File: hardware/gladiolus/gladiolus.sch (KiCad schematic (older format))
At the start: 94 parts, among them J1 NEIGHBOR1, J2 NEIGHBOR2, J7 BONUS_ROW, Q1 Q_NPN_BEC, U1 THS4520RGT, U2 AD8330ARQZ, U3 AD9283

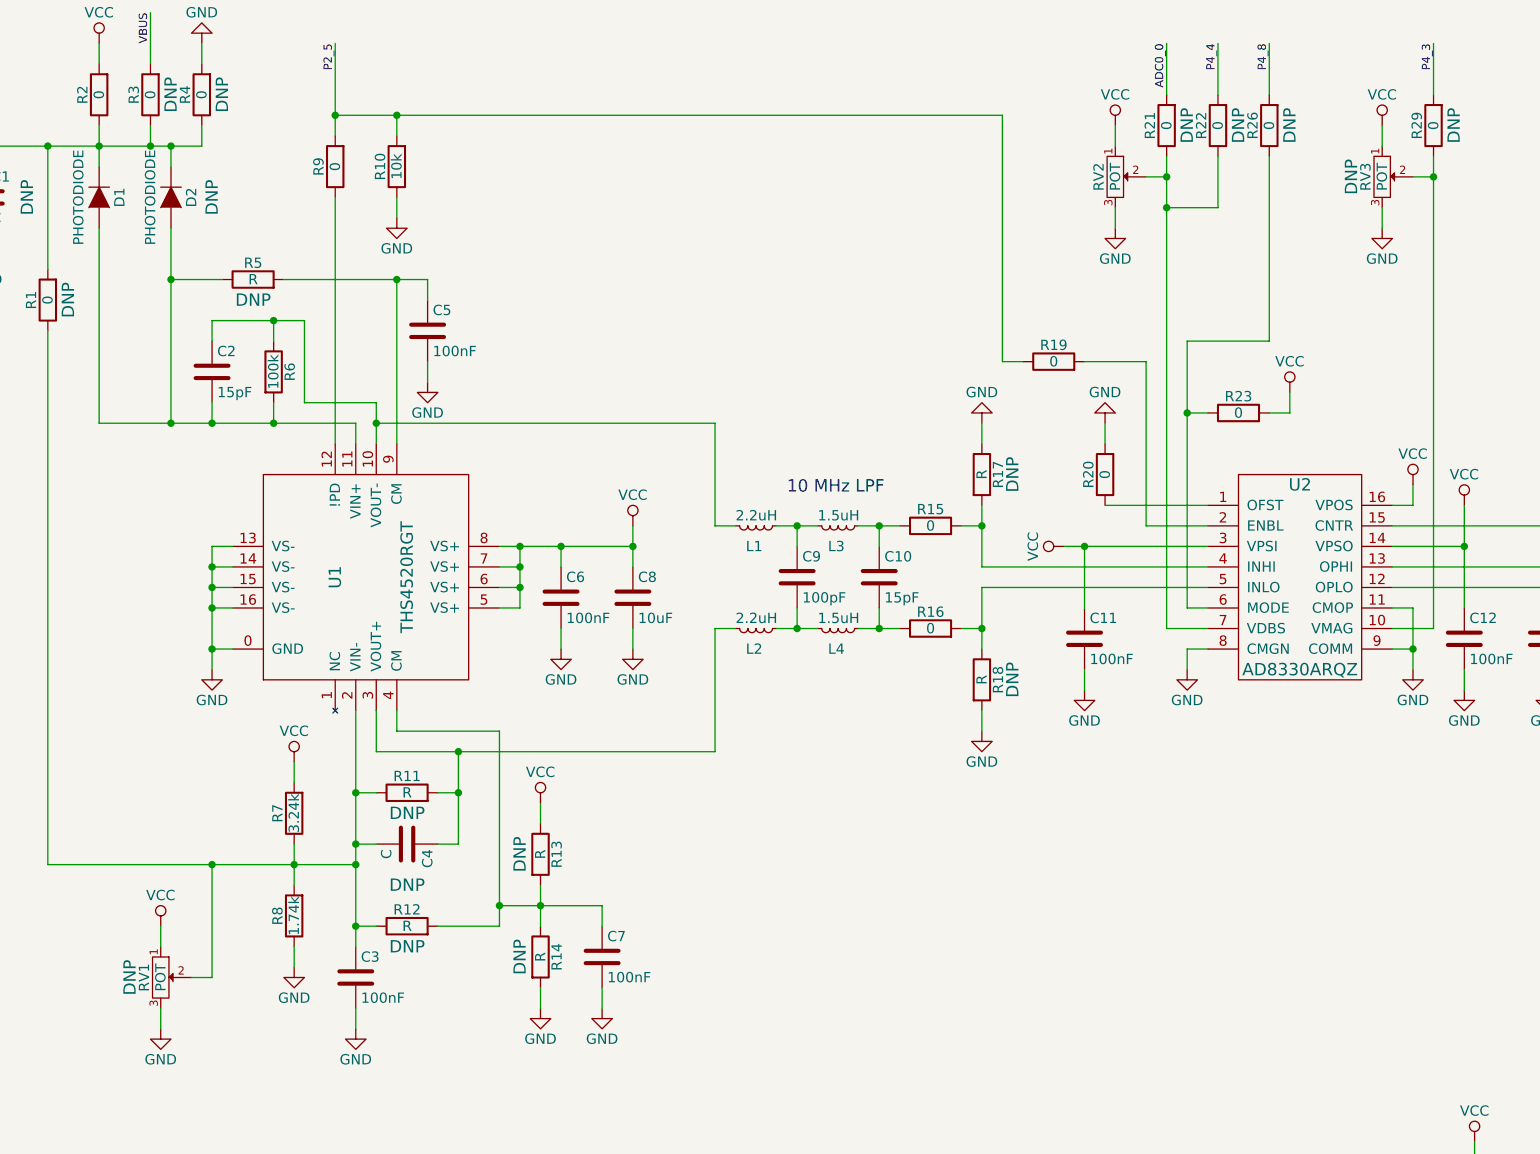
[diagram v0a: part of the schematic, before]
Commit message: Gladiolus: reversed potentiometers
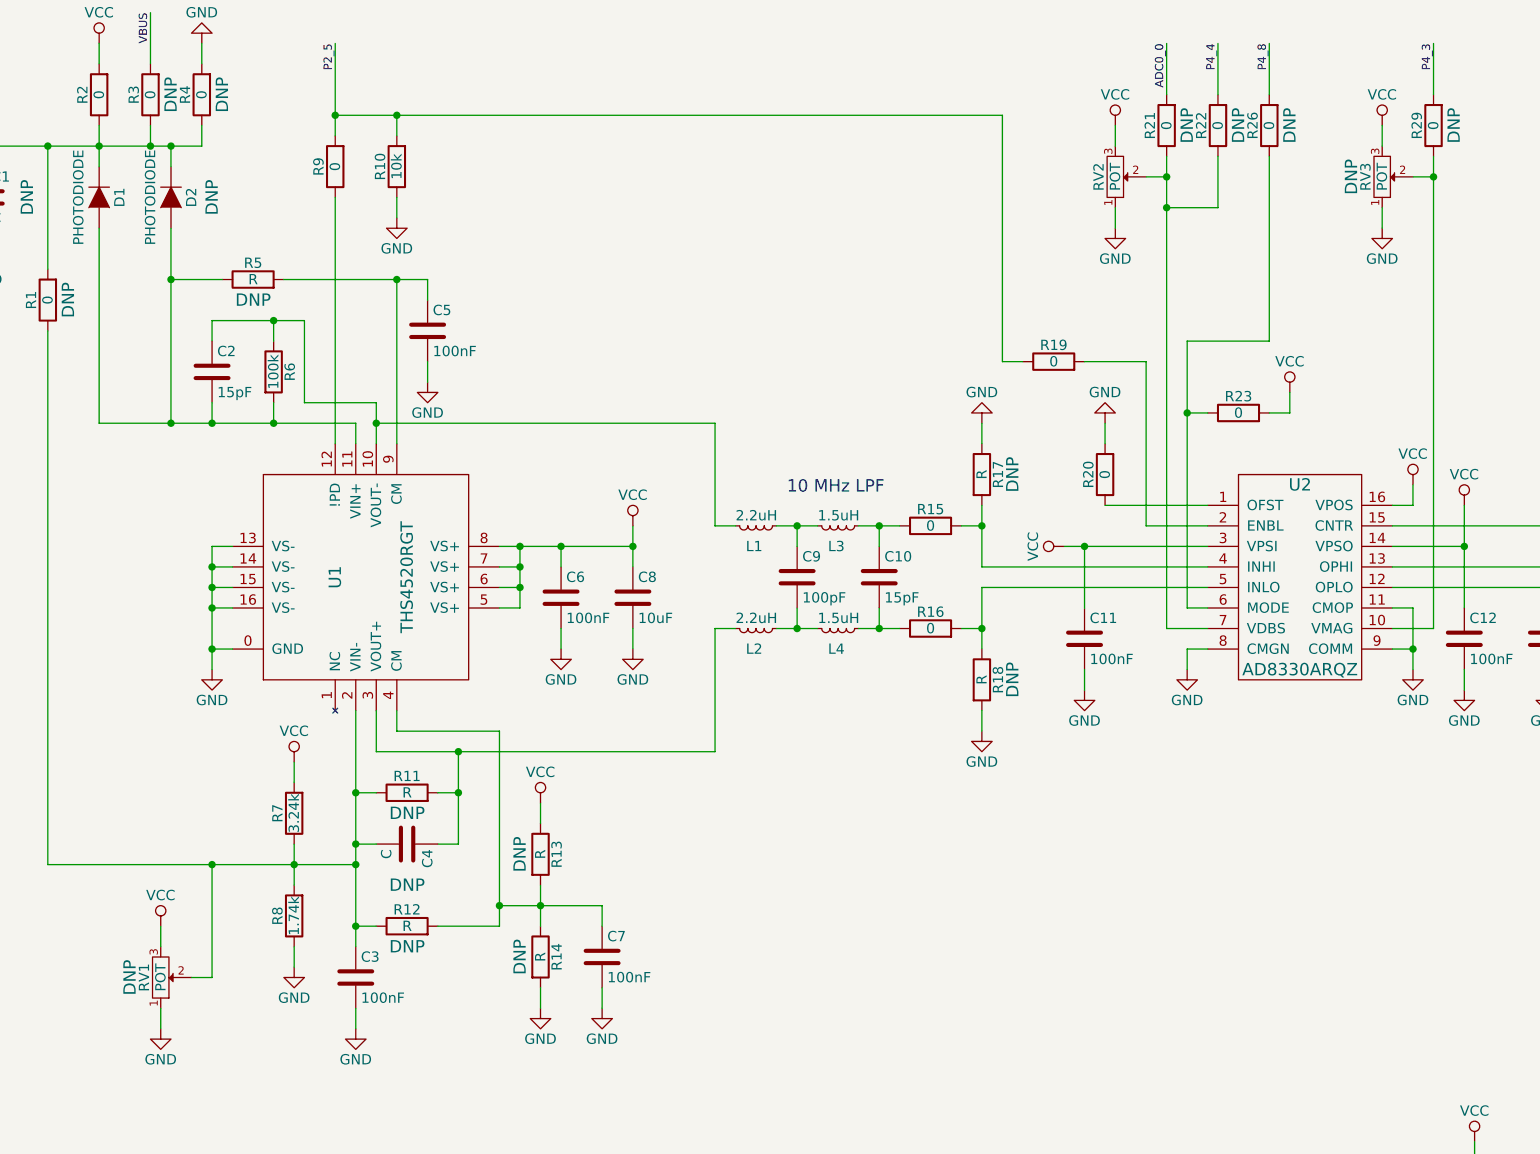
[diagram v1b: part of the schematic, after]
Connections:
- net GND: now also RV1.1, RV2.1, RV3.1; no longer RV1.3, RV2.3, RV3.3
- net VCC: now also RV1.3, RV2.3, RV3.3; no longer RV1.1, RV2.1, RV3.1
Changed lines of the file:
@@
 F 7 "DNP" H 7900 1800 60  0000 C CNN "Note"
 	1    7900 1950
-	0    1    1    0
+	0    1    -1   0
 $EndComp
 $Comp
@@
 F 6 "10k Ohm 0.2W, 1/5W PC Pins Through Hole Trimmer Potentiometer Cermet 1 Turn Top Adjustment" H 6600 1950 60  0001 C CNN "Description"
 	1    6600 1950
-	0    1    1    0
+	0    1    -1   0
 $EndComp
 $Comp
@@
 F 7 "DNP" H 1950 5700 60  0000 C CNN "Note"
 	1    1950 5850
-	0    1    1    0
+	0    1    -1   0
 $EndComp
 Text Label 13800 3100 2    40   ~ 0

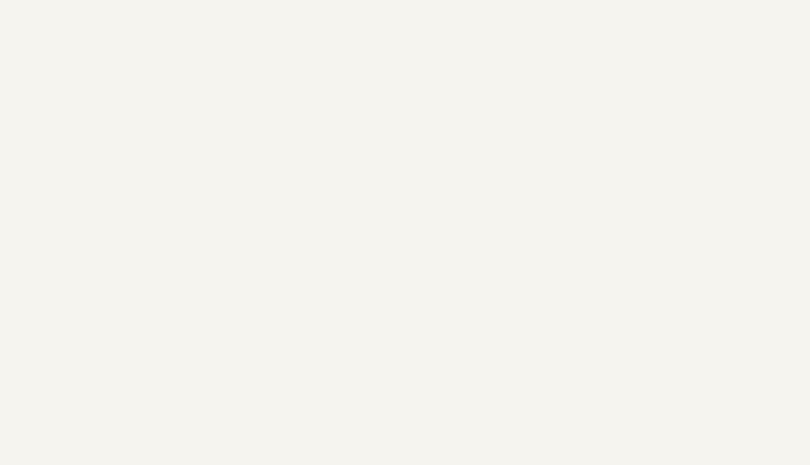
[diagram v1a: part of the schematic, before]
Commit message: Gladiolus: added female header to block direct TX to RX light
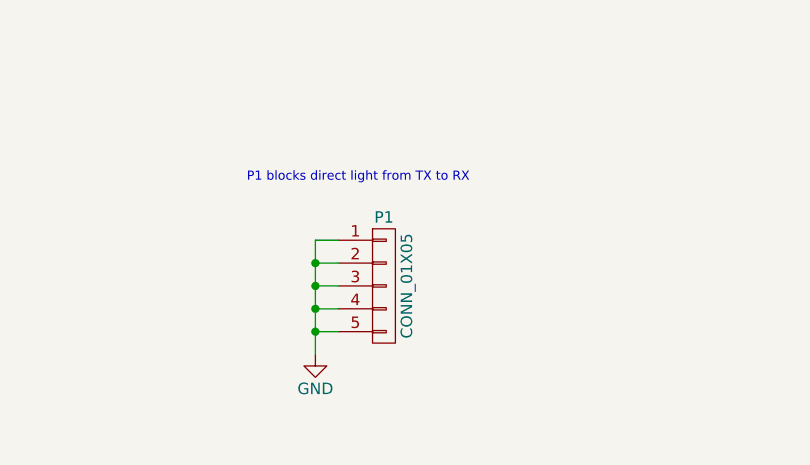
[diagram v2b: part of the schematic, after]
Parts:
- added P1: CONN_01X05, gsg-modules:HEADER-1x5, symbol CONN_01X05
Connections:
- net GND: now also P1.1 (P1), P1.2 (P2), P1.3 (P3), P1.4 (P4), P1.5 (P5)
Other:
- note added: "P1 blocks direct light from TX to RX"
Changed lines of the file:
@@
 Wire Wire Line
 	11600 4250 11600 5450
+$Comp
+L CONN_01X05 P1
+U 1 1 585CA618
+P 11600 7650
+F 0 "P1" H 11600 7950 50  0000 C CNN
+F 1 "CONN_01X05" V 11700 7650 50  0000 C CNN
+F 2 "gsg-modules:HEADER-1x5" H 11600 7650 50  0001 C CNN
+F 3 "" H 11600 7650 50  0000 C CNN
+F 4 "Sullins" H 11600 7650 60  0001 C CNN "Manufacturer"
+F 5 "PPTC051LFBN-RC" H 11600 7650 60  0001 C CNN "Part Number"
+F 6 "CONN HEADER FEM 5POS .1\" SGL TIN" H 11600 7650 60  0001 C CNN "Description"
+	1    11600 7650
+	1    0    0    -1
+$EndComp
+$Comp
+L GND #PWR060
+U 1 1 585CA943
+P 11300 7950
+F 0 "#PWR060" H 11300 7700 50  0001 C CNN
+F 1 "GND" H 11300 7800 50  0000 C CNN
+F 2 "" H 11300 7950 50  0000 C CNN
+F 3 "" H 11300 7950 50  0000 C CNN
+	1    11300 7950
+	1    0    0    -1
+$EndComp
+Wire Wire Line
+	11400 7450 11300 7450
+Wire Wire Line
+	11300 7450 11300 7950
+Wire Wire Line
+	11400 7550 11300 7550
+Connection ~ 11300 7550
+Wire Wire Line
+	11300 7650 11400 7650
+Connection ~ 11300 7650
+Wire Wire Line
+	11400 7750 11300 7750
+Connection ~ 11300 7750
+Wire Wire Line
+	11300 7850 11400 7850
+Connection ~ 11300 7850
+Text Notes 11000 7200 0    40   ~ 0
+P1 blocks direct light from TX to RX
 $EndSCHEMATC

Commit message: Gladiolus: corrected part selection for 0402 0 ohm resistors
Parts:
- R1, R19, R2, R20, R21, R22, R23, R24, R25, R26, R29, R3, R31, R4, R9: Description ES SMD 0.0OHM JUMPER 1/10W 0603 -> RES SMD 0.0OHM JUMPER 1/10W 0603
- R15, R16, R32, R33: Description ES SMD 0.0OHM JUMPER 1/10W 0603 -> RES SMD 0.0OHM JUMPER 1/16W 0402; Part Number RC0603JR-070RL -> RC0402JR-070RL
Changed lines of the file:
@@
 F 4 "Yageo" H 1650 1550 60  0001 C CNN "Manufacturer"
 F 5 "RC0603JR-070RL" H 1650 1550 60  0001 C CNN "Part Number"
-F 6 "ES SMD 0.0OHM JUMPER 1/10W 0603" H 1650 1550 60  0001 C CNN "Description"
+F 6 "RES SMD 0.0OHM JUMPER 1/10W 0603" H 1650 1550 60  0001 C CNN "Description"
 	1    1650 1550
 	-1   0    0    1
@@
 F 4 "Yageo" H 1900 1550 60  0001 C CNN "Manufacturer"
 F 5 "RC0603JR-070RL" H 1900 1550 60  0001 C CNN "Part Number"
-F 6 "ES SMD 0.0OHM JUMPER 1/10W 0603" H 1900 1550 60  0001 C CNN "Description"
+F 6 "RES SMD 0.0OHM JUMPER 1/10W 0603" H 1900 1550 60  0001 C CNN "Description"
 F 7 "DNP" V 1800 1550 60  0000 C CNN "Note"
 	1    1900 1550
@@
 F 4 "Yageo" H 2800 1900 60  0001 C CNN "Manufacturer"
 F 5 "RC0603JR-070RL" H 2800 1900 60  0001 C CNN "Part Number"
-F 6 "ES SMD 0.0OHM JUMPER 1/10W 0603" H 2800 1900 60  0001 C CNN "Description"
+F 6 "RES SMD 0.0OHM JUMPER 1/10W 0603" H 2800 1900 60  0001 C CNN "Description"
 	1    2800 1900
 	-1   0    0    1
@@
 F 4 "Yageo" H 7200 3100 60  0001 C CNN "Manufacturer"
 F 5 "RC0603JR-070RL" H 7200 3100 60  0001 C CNN "Part Number"
-F 6 "ES SMD 0.0OHM JUMPER 1/10W 0603" H 7200 3100 60  0001 C CNN "Description"
+F 6 "RES SMD 0.0OHM JUMPER 1/10W 0603" H 7200 3100 60  0001 C CNN "Description"
 	1    7200 3100
 	0    -1   -1   0
@@
 F 4 "Yageo" H 6300 2850 60  0001 C CNN "Manufacturer"
 F 5 "RC0603JR-070RL" H 6300 2850 60  0001 C CNN "Part Number"
-F 6 "ES SMD 0.0OHM JUMPER 1/10W 0603" H 6300 2850 60  0001 C CNN "Description"
+F 6 "RES SMD 0.0OHM JUMPER 1/10W 0603" H 6300 2850 60  0001 C CNN "Description"
 	1    6300 2850
 	0    -1   -1   0
@@
 F 4 "Yageo" H 6550 3400 60  0001 C CNN "Manufacturer"
 F 5 "RC0603JR-070RL" H 6550 3400 60  0001 C CNN "Part Number"
-F 6 "ES SMD 0.0OHM JUMPER 1/10W 0603" H 6550 3400 60  0001 C CNN "Description"
+F 6 "RES SMD 0.0OHM JUMPER 1/10W 0603" H 6550 3400 60  0001 C CNN "Description"
 	1    6550 3400
 	-1   0    0    1
@@
 F 3 "" H 10350 3650 50  0000 C CNN
 F 4 "Yageo" H 10350 3650 60  0001 C CNN "Manufacturer"
-F 5 "RC0603JR-070RL" H 10350 3650 60  0001 C CNN "Part Number"
-F 6 "ES SMD 0.0OHM JUMPER 1/10W 0603" H 10350 3650 60  0001 C CNN "Description"
+F 5 "RC0402JR-070RL" H 10350 3650 60  0001 C CNN "Part Number"
+F 6 "RES SMD 0.0OHM JUMPER 1/16W 0402" H 10350 3650 60  0001 C CNN "Description"
 	1    10350 3650
 	0    -1   -1   0
@@
 F 3 "" H 10350 4150 50  0000 C CNN
 F 4 "Yageo" H 10350 4150 60  0001 C CNN "Manufacturer"
-F 5 "RC0603JR-070RL" H 10350 4150 60  0001 C CNN "Part Number"
-F 6 "ES SMD 0.0OHM JUMPER 1/10W 0603" H 10350 4150 60  0001 C CNN "Description"
+F 5 "RC0402JR-070RL" H 10350 4150 60  0001 C CNN "Part Number"
+F 6 "RES SMD 0.0OHM JUMPER 1/16W 0402" H 10350 4150 60  0001 C CNN "Description"
 	1    10350 4150
 	0    -1   -1   0
@@
 F 4 "Yageo" H 9700 2750 60  0001 C CNN "Manufacturer"
 F 5 "RC0603JR-070RL" H 9700 2750 60  0001 C CNN "Part Number"
-F 6 "ES SMD 0.0OHM JUMPER 1/10W 0603" H 9700 2750 60  0001 C CNN "Description"
+F 6 "RES SMD 0.0OHM JUMPER 1/10W 0603" H 9700 2750 60  0001 C CNN "Description"
 	1    9700 2750
 	0    -1   -1   0
@@
 F 4 "Yageo" H 6850 1700 60  0001 C CNN "Manufacturer"
 F 5 "RC0603JR-070RL" H 6850 1700 60  0001 C CNN "Part Number"
-F 6 "ES SMD 0.0OHM JUMPER 1/10W 0603" H 6850 1700 60  0001 C CNN "Description"
+F 6 "RES SMD 0.0OHM JUMPER 1/10W 0603" H 6850 1700 60  0001 C CNN "Description"
 F 7 "DNP" V 6750 1700 60  0000 C CNN "Note"
 	1    6850 1700
@@
 F 4 "Yageo" H 7350 1700 60  0001 C CNN "Manufacturer"
 F 5 "RC0603JR-070RL" H 7350 1700 60  0001 C CNN "Part Number"
-F 6 "ES SMD 0.0OHM JUMPER 1/10W 0603" H 7350 1700 60  0001 C CNN "Description"
+F 6 "RES SMD 0.0OHM JUMPER 1/10W 0603" H 7350 1700 60  0001 C CNN "Description"
 F 7 "DNP" V 7250 1700 60  0000 C CNN "Note"
 	1    7350 1700
@@
 F 4 "Yageo" H 8150 1700 60  0001 C CNN "Manufacturer"
 F 5 "RC0603JR-070RL" H 8150 1700 60  0001 C CNN "Part Number"
-F 6 "ES SMD 0.0OHM JUMPER 1/10W 0603" H 8150 1700 60  0001 C CNN "Description"
+F 6 "RES SMD 0.0OHM JUMPER 1/10W 0603" H 8150 1700 60  0001 C CNN "Description"
 F 7 "DNP" V 8050 1700 60  0000 C CNN "Note"
 	1    8150 1700
@@
 F 4 "Yageo" H 2150 1550 60  0001 C CNN "Manufacturer"
 F 5 "RC0603JR-070RL" H 2150 1550 60  0001 C CNN "Part Number"
-F 6 "ES SMD 0.0OHM JUMPER 1/10W 0603" H 2150 1550 60  0001 C CNN "Description"
+F 6 "RES SMD 0.0OHM JUMPER 1/10W 0603" H 2150 1550 60  0001 C CNN "Description"
 F 7 "DNP" V 2050 1550 60  0000 C CNN "Note"
 	1    2150 1550
@@
 F 4 "Yageo" H 1400 2550 60  0001 C CNN "Manufacturer"
 F 5 "RC0603JR-070RL" H 1400 2550 60  0001 C CNN "Part Number"
-F 6 "ES SMD 0.0OHM JUMPER 1/10W 0603" H 1400 2550 60  0001 C CNN "Description"
+F 6 "RES SMD 0.0OHM JUMPER 1/10W 0603" H 1400 2550 60  0001 C CNN "Description"
 F 7 "DNP" V 1300 2550 60  0000 C CNN "Note"
 	1    1400 2550
@@
 F 3 "" H 5700 3650 50  0000 C CNN
 F 4 "Yageo" H 5700 3650 60  0001 C CNN "Manufacturer"
-F 5 "RC0603JR-070RL" H 5700 3650 60  0001 C CNN "Part Number"
-F 6 "ES SMD 0.0OHM JUMPER 1/10W 0603" H 5700 3650 60  0001 C CNN "Description"
+F 5 "RC0402JR-070RL" H 5700 3650 60  0001 C CNN "Part Number"
+F 6 "RES SMD 0.0OHM JUMPER 1/16W 0402" H 5700 3650 60  0001 C CNN "Description"
 	1    5700 3650
 	0    -1   -1   0
@@
 F 3 "" H 5700 4150 50  0000 C CNN
 F 4 "Yageo" H 5700 4150 60  0001 C CNN "Manufacturer"
-F 5 "RC0603JR-070RL" H 5700 4150 60  0001 C CNN "Part Number"
-F 6 "ES SMD 0.0OHM JUMPER 1/10W 0603" H 5700 4150 60  0001 C CNN "Description"
+F 5 "RC0402JR-070RL" H 5700 4150 60  0001 C CNN "Part Number"
+F 6 "RES SMD 0.0OHM JUMPER 1/16W 0402" H 5700 4150 60  0001 C CNN "Description"
 	1    5700 4150
 	0    -1   -1   0
@@
 F 4 "Yageo" H 7100 1700 60  0001 C CNN "Manufacturer"
 F 5 "RC0603JR-070RL" H 7100 1700 60  0001 C CNN "Part Number"
-F 6 "ES SMD 0.0OHM JUMPER 1/10W 0603" H 7100 1700 60  0001 C CNN "Description"
+F 6 "RES SMD 0.0OHM JUMPER 1/10W 0603" H 7100 1700 60  0001 C CNN "Description"
 F 7 "DNP" V 7000 1700 60  0000 C CNN "Note"
 	1    7100 1700
@@
 F 4 "Yageo" H 7300 7450 60  0001 C CNN "Manufacturer"
 F 5 "RC0603JR-070RL" H 7300 7450 60  0001 C CNN "Part Number"
-F 6 "ES SMD 0.0OHM JUMPER 1/10W 0603" H 7300 7450 60  0001 C CNN "Description"
+F 6 "RES SMD 0.0OHM JUMPER 1/10W 0603" H 7300 7450 60  0001 C CNN "Description"
 	1    7300 7450
 	0    -1   -1   0
@@
 F 4 "Yageo" H 7300 7650 60  0001 C CNN "Manufacturer"
 F 5 "RC0603JR-070RL" H 7300 7650 60  0001 C CNN "Part Number"
-F 6 "ES SMD 0.0OHM JUMPER 1/10W 0603" H 7300 7650 60  0001 C CNN "Description"
+F 6 "RES SMD 0.0OHM JUMPER 1/10W 0603" H 7300 7650 60  0001 C CNN "Description"
 F 7 "DNP" V 7200 7650 60  0000 C CNN "Note"
 	1    7300 7650

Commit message: Gladiolus: added TX DAC, changed TX GPIO pins
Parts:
- removed R24: 0, gsg-modules:0603, symbol R
- added C21, C22, C23, C24, C25, C27: 100nF, gsg-modules:0603, symbol C
- added C26: 15pF, gsg-modules:0402, symbol C
- added R28, R47, R48, R49, R50, R51, R52, R53, R54: 39, gsg-modules:0603, symbol R
- added R55, R58, R59, R60, R61, R62, R63: 10k, gsg-modules:0603, symbol R
- added R56, R65, R68: R, gsg-modules:0603, symbol R
- added R57: 2k, gsg-modules:0603, symbol R
- added R64, R66, R69: 250, gsg-modules:0603, symbol R
- added R67, R72, R74: 0, gsg-modules:0603, symbol R
- added R70: 953, gsg-modules:0603, symbol R
- added R71: 1000, gsg-modules:0603, symbol R
- added R73: 1k, gsg-modules:0603, symbol R
- added U4: AD9704, gsg-modules:QFN32-5, symbol AD9704
- added U5: LMH6643, gsg-modules:VSSOP8, symbol LMH6643
- R25: value 0 -> 1k; Description RES SMD 0.0OHM JUMPER 1/10W 0603 -> RES SMD 1K OHM 5% 1/10W 0603; Part Number RC0603JR-070RL -> RC0603JR-071KL
- R27: Note (none) -> DNP
- renumbered R28 to R24
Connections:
- net GND: now also R27.2, C21.2, C22.2, C23.2, C24.1, C25.2, C27.2, R56.2, R57.1, R59.2, R61.2, R63.2, R64.2, R66.2, R70.2, U4.0 (EPAD), U4.10 (DCOM), U4.14 (CLKCOM), U4.19 (OTCM), U4.22 (ACOM), U4.26 (DCOM), U5.4 (V-); no longer R27.1
- net P1_10: now also R50.2
- net P1_11: now also R49.2
- net P1_12: now also R48.2
- net P1_13: now also R47.2
- net P1_14: now also R28.2
- net P1_5: now also R24.2
- net P1_6: now also R54.2
- net P1_7: now also R53.2
- net P1_8: now also R52.2
- net P1_9: now also R51.2
- net P5_0: now also R55.2, U4.25 (SLEEP)
- net P5_2: now also R58.2, R59.1, U4.15 (CMODE)
- net P5_3: now also R60.2, R61.1, U4.16 (MODE)
- net P5_4: no longer R25.1
- net P5_5: now also R62.2, R63.1, U4.17 (PIN)
- net P5_6: now also R25.2
- net VCC: now also C21.1, C22.1, C23.1, C27.1, R55.1, R58.1, R60.1, R62.1, U4.11 (CLKVDD), U4.18 (AVDD), U4.3 (DVDD), U5.8 (V+)
- net at Q1.2 (E), R30.1: now also R74.2
- net at Q1.1 (B): now also R73.1; no longer R24.1
- new net: C25.1, R24.1, R25.1, R27.1, R65.2, R67.2, U5.3 (+INA)
- new net: R52.1, U4.1 (DB1)
- new net: R53.1, U4.2 (DB0)
- new net: R64.1, R65.1, U4.20 (IOUTB)
- new net: R66.1, R69.2, U4.21 (IOUTA)
- new net: C24.2, R67.1, R68.2, U4.23 (REFIO)
- new net: R57.2, U4.24 (FS_ADJ)
- new net: R28.1, U4.27 (DB7)
- new net: R47.1, U4.28 (DB6)
- new net: R48.1, U4.29 (DB5)
- new net: R49.1, U4.30 (DB4)
- new net: R50.1, U4.31 (DB3)
- new net: R51.1, U4.32 (DB2)
- new net: C26.2, R71.2, R72.1, U5.1 (OUTA)
- new net: C26.1, R68.1, R69.1, R70.1, R71.1, U5.2 (-INA)
- new net: R72.2, U5.5 (+INB)
- new net: R74.1, U5.6 (-INB)
- new net: R73.2, U5.7 (OUTB)
- new net DACCLK: R54.1, R56.1, U4.12 (CLK+)
- no-connect marks 1 -> 2
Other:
- note added: "Default configuration:\npin mode\nunsigned binary\nsingle-ended clock"
- note added: "GPIO1[0]"
- note added: "GPIO1[1]"
- note added: "GPIO1[2]"
- note added: "GPIO1[3]"
- note added: "GPIO1[4]"
- note added: "GPIO1[5]"
- note added: "GPIO1[6]"
- note added: "GPIO1[7]"
- note added: "GPIO1[8]"
- note added: "GPIO1[9]"
- note added: "GPIO2[11]"
- note added: "GPIO2[12]"
- note added: "GPIO2[14]"
- note added: "GPIO2[15]"
- note added: "GPIO2[9]"
- note removed: "TODO:\nAD9704 DAC\nreconstruction filter\nLMH6643 dual op-amp\nNPN"
- moved on the sheet: C1, C10, C11, C12, C13, C14, C15, C16, C17, C18, C19, C2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

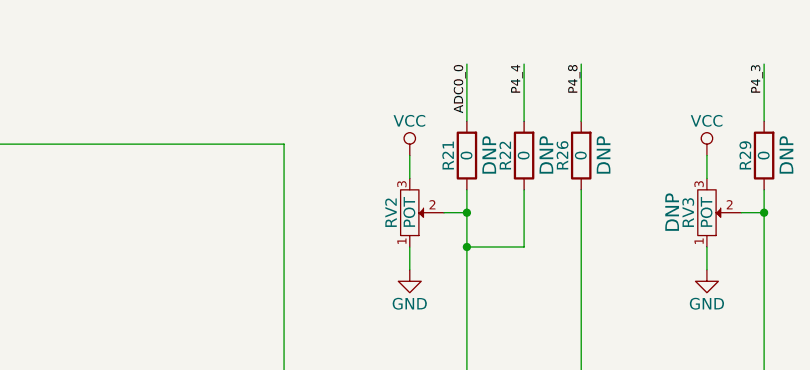
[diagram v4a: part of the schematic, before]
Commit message: Gladiolus: corrected voltage range of RV2
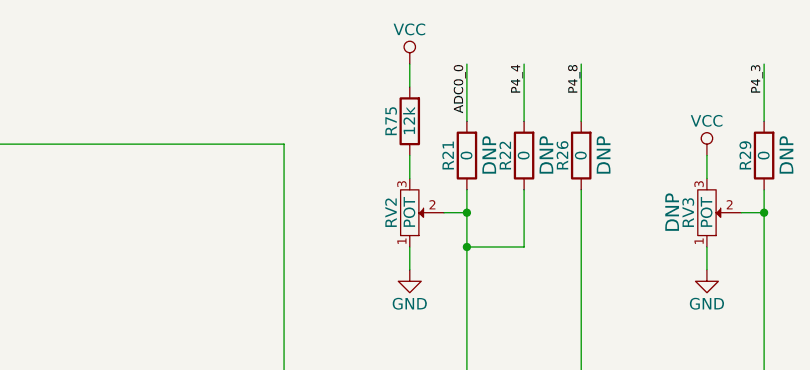
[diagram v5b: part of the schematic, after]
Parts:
- added R75: 12k, gsg-modules:0603, symbol R
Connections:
- net VCC: now also R75.2; no longer RV2.3
- new net: R75.1, RV2.3
